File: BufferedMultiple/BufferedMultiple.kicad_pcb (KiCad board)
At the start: 2 copper layers, 26 parts

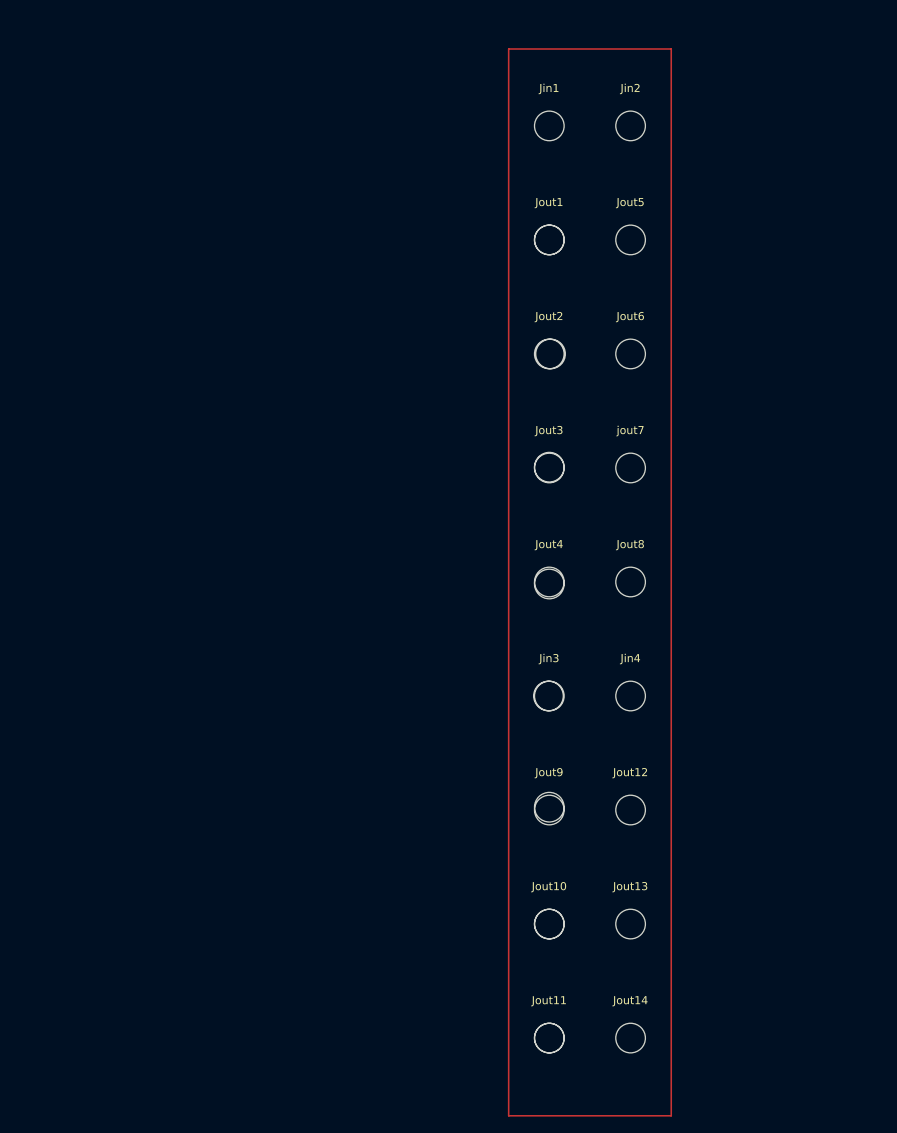
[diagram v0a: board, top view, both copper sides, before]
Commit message: remove simulation.  added project level symbols and footprints
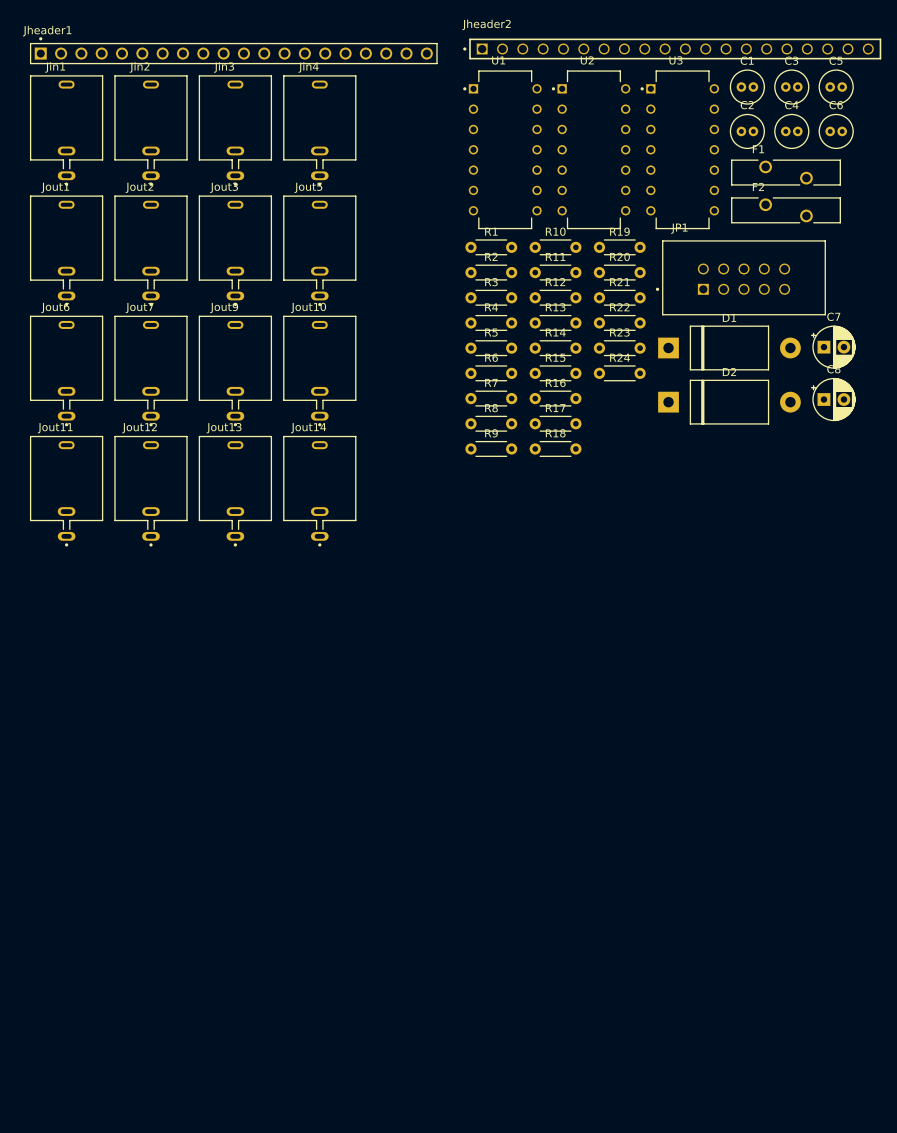
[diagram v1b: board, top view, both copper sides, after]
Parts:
- removed ? (x8): , 
- removed Jout4, Jout8, jout7: MountingHole_3.7mm, MountingHole:MountingHole_3.7mm
- added C1: 0.1uf, Capacitor_THT:C_Radial_D4.0mm_H5.0mm_P1.50mm, F.Cu at (165.0, 39.7)
- added C2: 0.1uf, Capacitor_THT:C_Radial_D4.0mm_H5.0mm_P1.50mm, F.Cu at (165.0, 45.2)
- added C3: 0.1uf, Capacitor_THT:C_Radial_D4.0mm_H5.0mm_P1.50mm, F.Cu at (170.5, 39.7)
- added C4: 0.1uf, Capacitor_THT:C_Radial_D4.0mm_H5.0mm_P1.50mm, F.Cu at (170.5, 45.2)
- added C5: 0.1uf, Capacitor_THT:C_Radial_D4.0mm_H5.0mm_P1.50mm, F.Cu at (176.1, 39.7)
- added C6: 0.1uf, Capacitor_THT:C_Radial_D4.0mm_H5.0mm_P1.50mm, F.Cu at (176.1, 45.2)
- added C7: 10uf, Capacitor_THT:CP_Radial_D5.0mm_P2.50mm, F.Cu at (175.3, 72.2)
- added C8: 10uf, Capacitor_THT:CP_Radial_D5.0mm_P2.50mm, F.Cu at (175.3, 78.7)
- added D1: 1N5934B, 1N5934B:P2_DO-201, F.Cu at (163.5, 72.3)
- added D2: 1N5934B, 1N5934B:P2_DO-201, F.Cu at (163.5, 79.1)
- added F1: type="R" model="Polyfuse" lib="", 72R020XU:FUSRB510W81L1358T310H1980, F.Cu at (170.6, 50.4)
- added F2: type="R" model="Polyfuse" lib="", 72R020XU:FUSRB510W81L1358T310H1980, F.Cu at (170.6, 55.1)
- added JP1: 1761681-3, 1761681-3:TE_1761681-3, F.Cu at (160.2, 65.0)
- added Jheader1: 2-826646-0, 2-826646-0:TE_2-826646-0, F.Cu at (101.5, 35.5)
- added Jheader2: ESQ-120-12-T-S, ESQ-120-12-T-S:SAMTEC_ESQ-120-12-T-S, F.Cu at (132.6, 34.9)
- added Jout7: PJ398SM-12, Thonk_PJ398SM:THONK_PJ398SM-12, F.Cu at (91.2, 74.3)
- added R1: 1k, Resistor_THT:R_Axial_DIN0204_L3.6mm_D1.6mm_P5.08mm_Horizontal, F.Cu at (131.2, 59.7)
- added R10: 100k, Resistor_THT:R_Axial_DIN0204_L3.6mm_D1.6mm_P5.08mm_Horizontal, F.Cu at (139.2, 59.7)
- added R11: 1k, Resistor_THT:R_Axial_DIN0204_L3.6mm_D1.6mm_P5.08mm_Horizontal, F.Cu at (139.2, 62.9)
- added R12: 1k, Resistor_THT:R_Axial_DIN0204_L3.6mm_D1.6mm_P5.08mm_Horizontal, F.Cu at (139.2, 66.0)
- added R13: 1k, Resistor_THT:R_Axial_DIN0204_L3.6mm_D1.6mm_P5.08mm_Horizontal, F.Cu at (139.2, 69.2)
- added R14: 1k, Resistor_THT:R_Axial_DIN0204_L3.6mm_D1.6mm_P5.08mm_Horizontal, F.Cu at (139.2, 72.3)
- added R15: 1M, Resistor_THT:R_Axial_DIN0204_L3.6mm_D1.6mm_P5.08mm_Horizontal, F.Cu at (139.2, 75.5)
- added R16: 100k, Resistor_THT:R_Axial_DIN0204_L3.6mm_D1.6mm_P5.08mm_Horizontal, F.Cu at (139.2, 78.6)
- added R17: 100k, Resistor_THT:R_Axial_DIN0204_L3.6mm_D1.6mm_P5.08mm_Horizontal, F.Cu at (139.2, 81.8)
- added R18: 100k, Resistor_THT:R_Axial_DIN0204_L3.6mm_D1.6mm_P5.08mm_Horizontal, F.Cu at (139.2, 84.9)
- added R19: 100k, Resistor_THT:R_Axial_DIN0204_L3.6mm_D1.6mm_P5.08mm_Horizontal, F.Cu at (147.2, 59.7)
- added R2: 1k, Resistor_THT:R_Axial_DIN0204_L3.6mm_D1.6mm_P5.08mm_Horizontal, F.Cu at (131.2, 62.9)
- added R20: 100k, Resistor_THT:R_Axial_DIN0204_L3.6mm_D1.6mm_P5.08mm_Horizontal, F.Cu at (147.2, 62.9)
- added R21: 100k, Resistor_THT:R_Axial_DIN0204_L3.6mm_D1.6mm_P5.08mm_Horizontal, F.Cu at (147.2, 66.0)
- added R22: 100k, Resistor_THT:R_Axial_DIN0204_L3.6mm_D1.6mm_P5.08mm_Horizontal, F.Cu at (147.2, 69.2)
- added R23: 100k, Resistor_THT:R_Axial_DIN0204_L3.6mm_D1.6mm_P5.08mm_Horizontal, F.Cu at (147.2, 72.3)
- added R24: 100k, Resistor_THT:R_Axial_DIN0204_L3.6mm_D1.6mm_P5.08mm_Horizontal, F.Cu at (147.2, 75.5)
- added R3: 1k, Resistor_THT:R_Axial_DIN0204_L3.6mm_D1.6mm_P5.08mm_Horizontal, F.Cu at (131.2, 66.0)
- added R4: 1k, Resistor_THT:R_Axial_DIN0204_L3.6mm_D1.6mm_P5.08mm_Horizontal, F.Cu at (131.2, 69.2)
- added R5: 1k, Resistor_THT:R_Axial_DIN0204_L3.6mm_D1.6mm_P5.08mm_Horizontal, F.Cu at (131.2, 72.3)
- added R6: 1k, Resistor_THT:R_Axial_DIN0204_L3.6mm_D1.6mm_P5.08mm_Horizontal, F.Cu at (131.2, 75.5)
- added R7: 1k, Resistor_THT:R_Axial_DIN0204_L3.6mm_D1.6mm_P5.08mm_Horizontal, F.Cu at (131.2, 78.6)
- added R8: 1k, Resistor_THT:R_Axial_DIN0204_L3.6mm_D1.6mm_P5.08mm_Horizontal, F.Cu at (131.2, 81.8)
- added R9: 100k, Resistor_THT:R_Axial_DIN0204_L3.6mm_D1.6mm_P5.08mm_Horizontal, F.Cu at (131.2, 84.9)
- added U1: TL074CN, TL074CN:DIP794W45P254L1969H508Q14, F.Cu at (135.5, 47.5)
- added U2: TL074CN, TL074CN:DIP794W45P254L1969H508Q14, F.Cu at (146.5, 47.5)
- added U3: TL074CN, TL074CN:DIP794W45P254L1969H508Q14, F.Cu at (157.6, 47.5)
- Jin1, Jin2, Jin3, Jin4, Jout1, Jout10, Jout11, Jout12, Jout13, Jout14, Jout2, Jout3, Jout5, Jout6, Jout9: value MountingHole_3.7mm -> PJ398SM-12; footprint MountingHole:MountingHole_3.7mm -> Thonk_PJ398SM:THONK_PJ398SM-12
- moved Jout11 91.8 mm to (80.6, 89.4)
- moved Jin3 81.6 mm to (101.7, 44.3)
- moved Jin4 81.4 mm to (112.3, 44.3)
- moved Jout14 79.4 mm to (112.3, 89.4)
- moved Jout10 75.6 mm to (112.3, 74.3)
- moved Jout13 73.9 mm to (101.7, 89.4)
- moved Jout12 72.5 mm to (91.2, 89.4)
- moved Jout6 70.5 mm to (80.6, 74.3)
- moved Jout9 68.1 mm to (101.7, 74.3)
- moved Jout1 60.3 mm to (80.6, 59.3)
- moved Jin1 60.3 mm to (80.6, 44.3)
- moved Jin2 60.0 mm to (91.2, 44.3)
- moved Jout2 51.6 mm to (91.2, 59.3)
- moved Jout3 48.2 mm to (101.7, 59.3)
- moved Jout5 38.9 mm to (112.3, 59.3)
